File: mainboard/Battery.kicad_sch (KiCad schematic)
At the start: 23 parts, among them IC701 BQ21040DBV, IC702 MCP3425A2, Q701 BSS138, Q702 BSS84, X701 USB

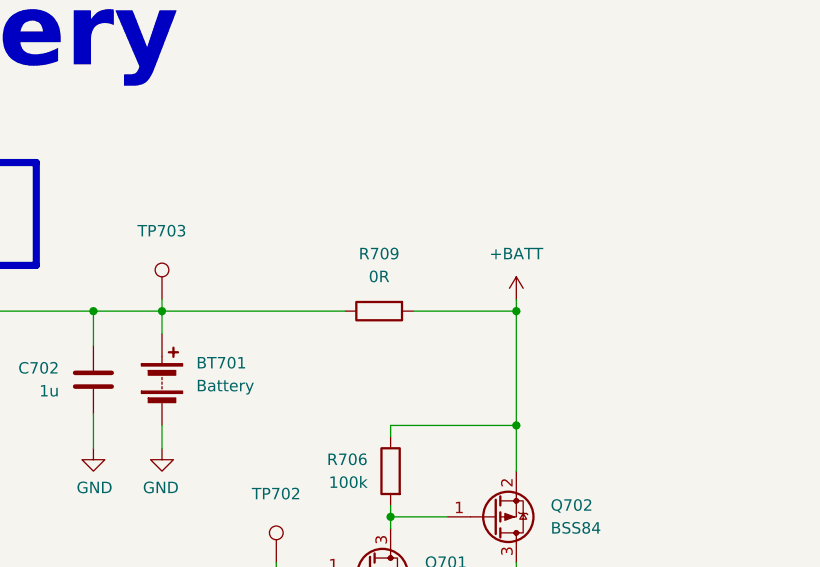
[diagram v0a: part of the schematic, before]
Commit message: Continue routing, add flash LEDs for the RGB camera, add PWM controller for the Display Backlight and the flash LEDs, add Polyfuse for the battery
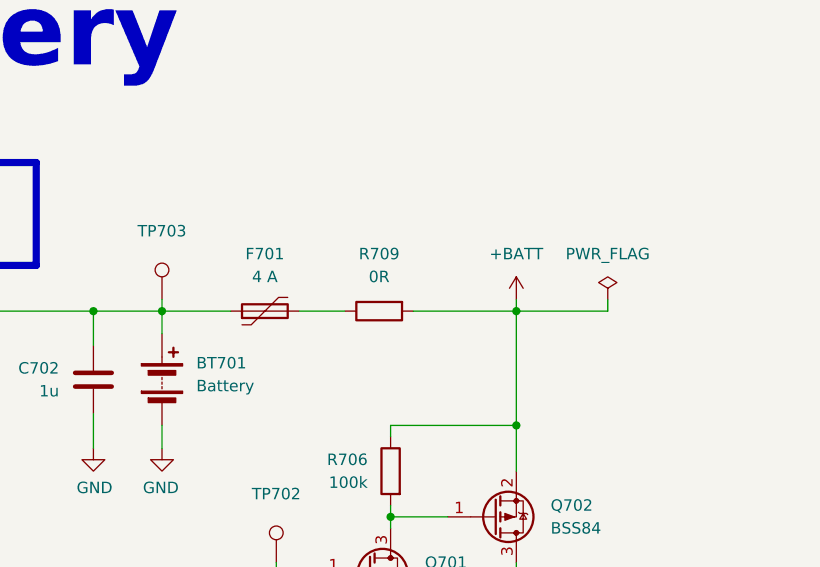
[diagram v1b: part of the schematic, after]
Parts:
- added F701: 4 A, Fuse:Fuse_1206_3216Metric, symbol Device:Polyfuse
- R709: footprint Resistor_SMD:R_0603_1608Metric -> Resistor_SMD:R_1206_3216Metric; manf (none) -> Bourns; manf# (none) -> CR1206-J/-000ELF; mouser# (none) -> 652-CR1206-J/-000ELF
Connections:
- net at BT701.1 (+), C702.1, IC701.2 (OUT)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: now also F701.1; no longer R709.1
- new net: F701.2, R709.1
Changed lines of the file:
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@@
 	(wire
 		(pts
-			(xy 193.04 50.8) (xy 213.36 50.8)
+			(xy 193.04 50.8) (xy 200.66 50.8)
 		)
 		(stroke
@@
 	(wire
 		(pts
+			(xy 208.28 50.8) (xy 213.36 50.8)
+		)
+		(stroke
+			(width 0)
+			(type default)
+		)
+	)
+	(wire
+		(pts
 			(xy 213.36 137.16) (xy 213.36 146.05)
 		)
@@
 	(wire
 		(pts
+			(xy 242.57 50.8) (xy 242.57 49.53)
+		)
+		(stroke
+			(width 0)
+			(type default)
+		)
+	)
+	(wire
+		(pts
 			(xy 97.79 82.55) (xy 97.79 81.28)
 		)
@@
 	(wire
 		(pts
+			(xy 232.41 50.8) (xy 242.57 50.8)
+		)
+		(stroke
+			(width 0)
+			(type default)
+		)
+	)
+	(wire
+		(pts
 			(xy 80.01 63.5) (xy 78.74 63.5)
 		)
@@
 	)
 	(symbol
+		(lib_id "power:PWR_FLAG")
+		(at 242.57 49.53 0)
+		(unit 1)
+		(exclude_from_sim no)
+		(in_bom yes)
+		(on_board yes)
+		(dnp no)
+		(fields_autoplaced yes)
+		(property "Reference" "#FLG0702"
+			(at 242.57 47.625 0)
+			(effects
+				(font
+					(size 1.27 1.27)
+				)
+				(hide yes)
+			)
+		)
+		(property "Value" "PWR_FLAG"
+			(at 242.57 44.45 0)
+			(effects
+				(font
+					(size 1.27 1.27)
+				)
+			)
+		)
+		(property "Footprint" ""
+			(at 242.57 49.53 0)
+			(effects
+				(font
+					(size 1.27 1.27)
+				)
+				(hide yes)
+			)
+		)
+		(property "Datasheet" "~"
+			(at 242.57 49.53 0)
+			(effects
+				(font
+					(size 1.27 1.27)
+				)
+				(hide yes)
+			)
+		)
+		(property "Description" "Special symbol for telling ERC where power comes from"
+			(at 242.57 49.53 0)
+			(effects
+				(font
+					(size 1.27 1.27)
+				)
+				(hide yes)
+			)
+		)
+		(pin "1"
+		)
+		(instances
+			(project "Mainboard"
+				(path "/d5742f03-3b1a-42e5-a384-018bd4b919aa/c5103ceb-5325-4a84-a025-9638a412984e/a86b9e25-5bc0-455f-833c-d00b4e9a8b22"
+					(reference "#FLG0702")
+					(unit 1)
+				)
+			)
+		)
+	)
+	(symbol
 		(lib_id "Device:R")
 		(at 132.08 60.96 0)
@@
 	)
 	(symbol
+		(lib_id "Device:Polyfuse")
+		(at 204.47 50.8 90)
+		(unit 1)
+		(exclude_from_sim no)
+		(in_bom yes)
+		(on_board yes)
+		(dnp no)
+		(fields_autoplaced yes)
+		(property "Reference" "F701"
+			(at 204.47 44.45 90)
+			(effects
+				(font
+					(size 1.27 1.27)
+				)
+			)
+		)
+		(property "Value" "4 A"
+			(at 204.47 46.99 90)
+			(effects
+				(font
+					(size 1.27 1.27)
+				)
+			)
+		)
+		(property "Footprint" "Fuse:Fuse_1206_3216Metric"
+			(at 209.55 49.53 0)
+			(effects
+				(font
+					(size 1.27 1.27)
+				)
+				(justify left)
+				(hide yes)
+			)
+		)
+		(property "Datasheet" "https://www.mouser.de/manufacturer/littelfuse/"
+			(at 204.47 50.8 0)
+			(effects
+				(font
+					(size 1.27 1.27)
+				)
+				(hide yes)
+			)
+		)
+		(property "Description" "Resettable fuse, polymeric positive temperature coefficient"
+			(at 204.47 50.8 0)
+			(effects
+				(font
+					(size 1.27 1.27)
+				)
+				(hide yes)
+			)
+		)
+		(property "manf" "Littelfuse"
+			(at 204.47 50.8 0)
+			(effects
+				(font
+					(size 1.27 1.27)
+				)
+				(hide yes)
+			)
+		)
+		(property "manf#" "1206L400SLWR"
+			(at 204.47 50.8 0)
+			(effects
+				(font
+					(size 1.27 1.27)
+				)
+				(hide yes)
+			)
+		)
+		(property "mouser#" "576-1206L400SLWR"
+			(at 204.47 50.8 0)
+			(effects
+				(font
+					(size 1.27 1.27)
+				)
+				(hide yes)
+			)
+		)
+		(property "CONFIG" ""
+			(at 204.47 50.8 0)
+			(effects
+				(font
+					(size 1.27 1.27)
+				)
+				(hide yes)
+			)
+		)
+		(pin "2"
+		)
+		(pin "1"
+		)
+		(instances
+			(project ""
+				(path "/d5742f03-3b1a-42e5-a384-018bd4b919aa/c5103ceb-5325-4a84-a025-9638a412984e/a86b9e25-5bc0-455f-833c-d00b4e9a8b22"
+					(reference "F701")
+					(unit 1)
+				)
+			)
+		)
+	)
+	(symbol
 		(lib_id "power:GND")
 		(at 213.36 146.05 0)
@@
 			)
 		)
-		(property "Footprint" "Resistor_SMD:R_0603_1608Metric"
+		(property "Footprint" "Resistor_SMD:R_1206_3216Metric"
 			(at 217.17 49.022 90)
 			(effects
@@
 			)
 		)
-		(property "Datasheet" "https://www.mouser.de/datasheet/2/54/cr-1858361.pdf"
+		(property "Datasheet" "https://www.mouser.de/datasheet/3/40/1/cr.pdf"
 			(at 217.17 50.8 0)
 			(effects
@@
 			)
 		)
-		(property "manf" ""
+		(property "manf" "Bourns"
 			(at 217.17 50.8 0)
 			(effects
@@
 			)
 		)
-		(property "manf#" ""
+		(property "manf#" "CR1206-J/-000ELF"
 			(at 217.17 50.8 0)
 			(effects
@@
 			)
 		)
-		(property "mouser#" ""
+		(property "mouser#" "652-CR1206-J/-000ELF"
 			(at 217.17 50.8 0)
 			(effects

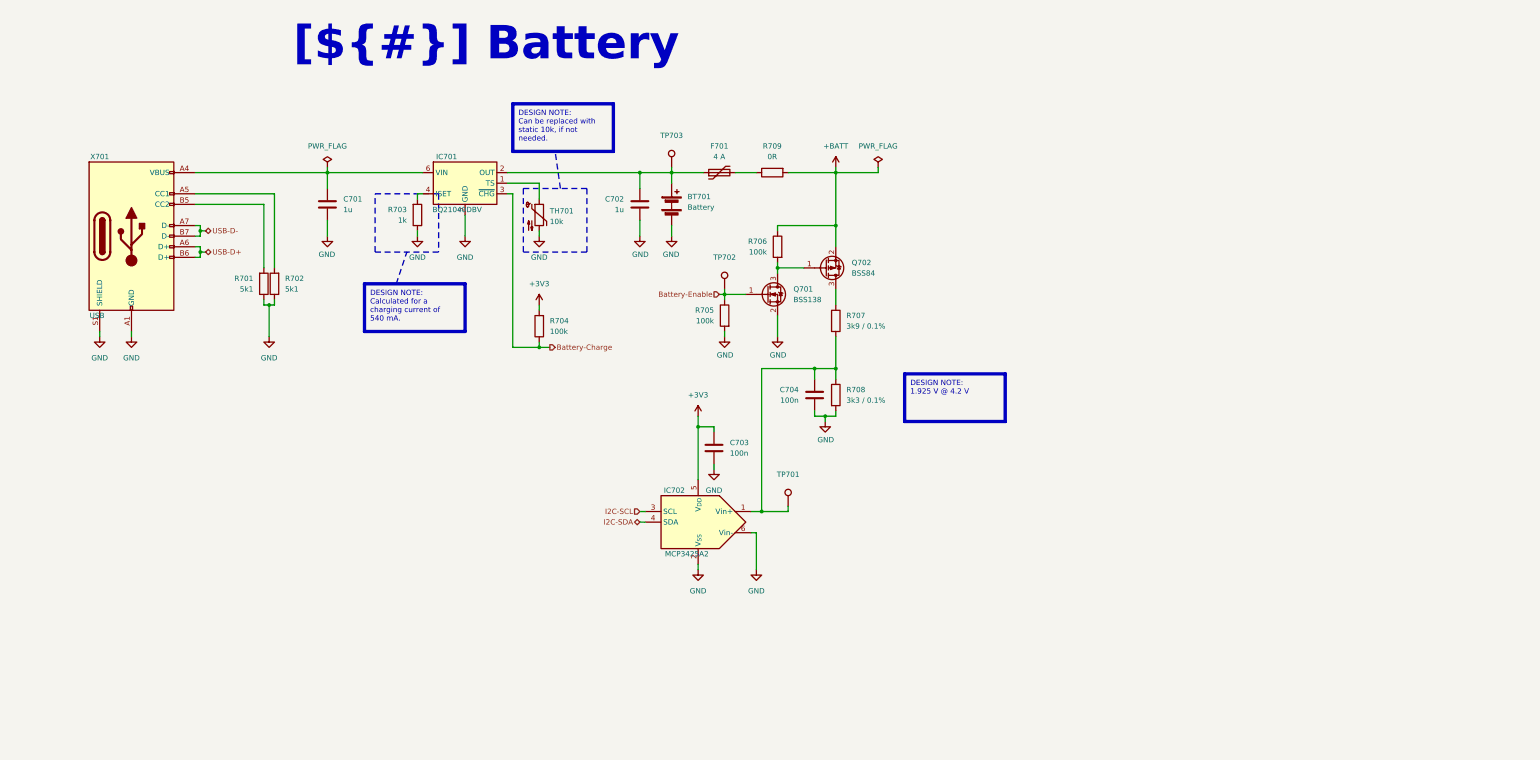
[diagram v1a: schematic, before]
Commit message: Remove ADC for battery measurement and add a fuel gauge
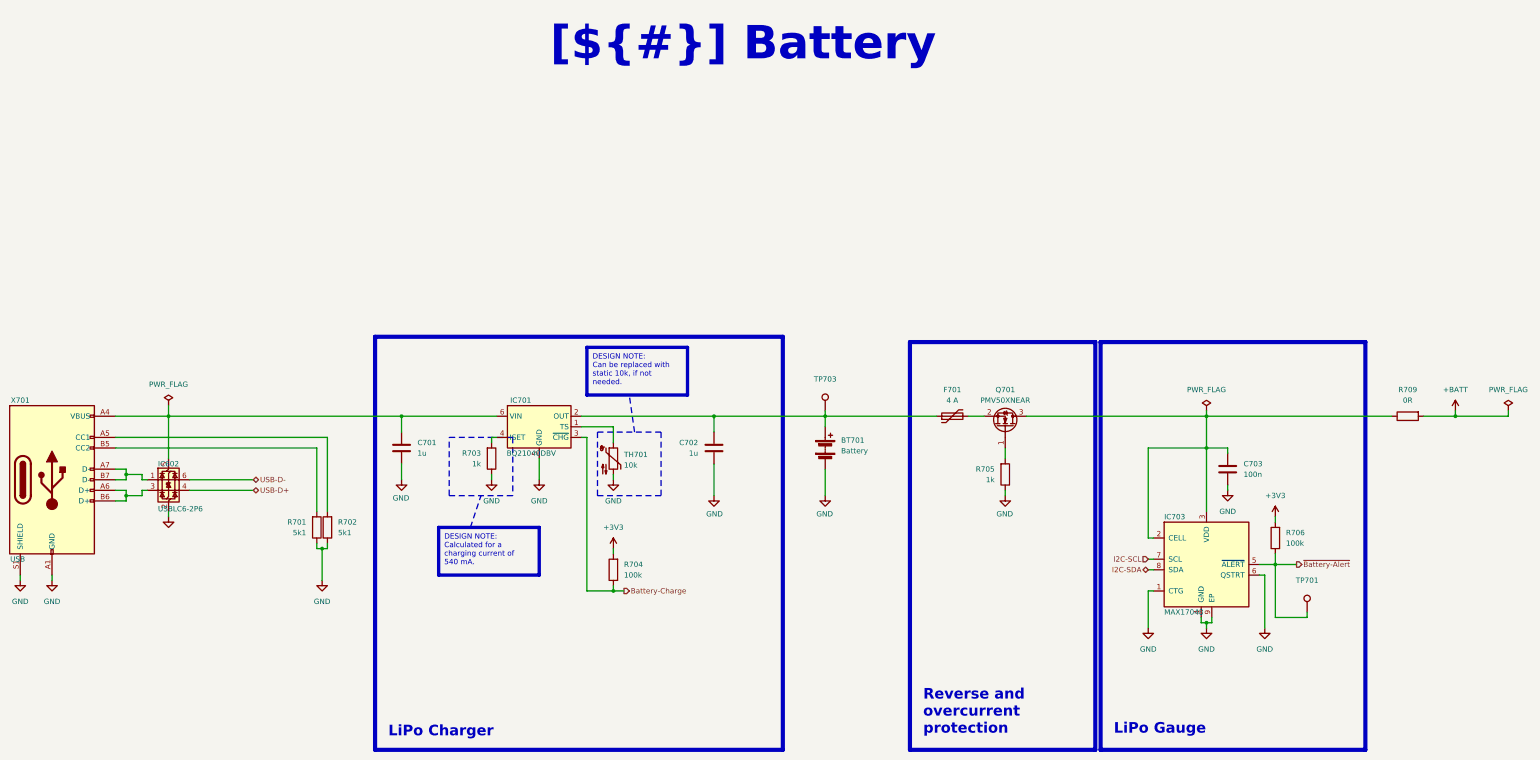
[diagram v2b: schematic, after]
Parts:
- removed C704: 100n, Capacitor_SMD:C_0603_1608Metric, symbol Device:C
- removed IC702: MCP3425A2, Package_TO_SOT_SMD:SOT-23-6, symbol Analog_ADC:MCP3425Axx-xCH
- removed Q701: BSS138, Package_TO_SOT_SMD:SOT-23, symbol Transistor_FET:BSS138
- removed Q702: BSS84, Package_TO_SOT_SMD:SOT-23, symbol Transistor_FET:BSS84
- removed R707: 3k9 / 0.1%, Resistor_SMD:R_0603_1608Metric, symbol Device:R
- removed R708: 3k3 / 0.1%, Resistor_SMD:R_0603_1608Metric, symbol Device:R
- removed TP702: ~, TestPoint:TestPoint_Pad_1.0x1.0mm, symbol Connector:TestPoint
- added IC602: USBLC6-2P6, Package_TO_SOT_SMD:SOT-666, symbol Power_Protection:USBLC6-2P6
- added IC703: MAX17048, Package_DFN_QFN:TDFN-8-1EP_2x2mm_P0.5mm_EP0.8x1.2mm, symbol Maxim:MAX17048
- added Q701: PMV50XNEAR, Package_TO_SOT_SMD:SOT-23, symbol Nexperia:PMV50XNEAR
- R705: value 100k -> 1k; manf# CR0603-JW-104ELF -> CR0603-JW-102ELF; mouser# 652-CR0603-JW-104ELF -> 652-CR0603-JW-102ELF
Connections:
- net Battery-Enable is gone; now on net GND: R705.1
- net +3V3: now also R706.2; no longer C703.1
- net +BATT: no longer R706.1
- net GND: now also IC602.2 (GND), IC703.1 (CTG), IC703.4 (GND), IC703.6 (QSTRT), IC703.9 (EP); no longer R705.2
- net I2C-SCL: now also IC703.7 (SCL)
- net I2C-SDA: now also IC703.8 (SDA)
- net USB-D+: now also IC602.4 (I/O2); no longer X701.A6 (D+), X701.B6 (D+)
- net USB-D-: now also IC602.6 (I/O1); no longer X701.A7 (D-), X701.B7 (D-)
- net ~{Battery-Alert}: now reaches TP701.1
- net ~{Battery-Alert}: now also R706.1, IC703.5 (~{ALERT})
- net at C701.1, IC701.6 (VIN), X701.A4 (VBUS)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: now also IC602.5 (VBUS)
- net at F701.2: now also Q701.2 (S); no longer R709.1
- new net: IC602.1 (I/O1), X701.A7 (D-), X701.B7 (D-)
- new net: IC602.3 (I/O2), X701.A6 (D+), X701.B6 (D+)
- new net: Q701.1 (G), R705.2
- new net: C703.1, IC703.2 (CELL), IC703.3 (VDD), Q701.3 (D), R709.1
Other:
- moved on the sheet: BT701, C701, C702, F701, IC701, R701, R702, R703, R704, R709, TH701, TP703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

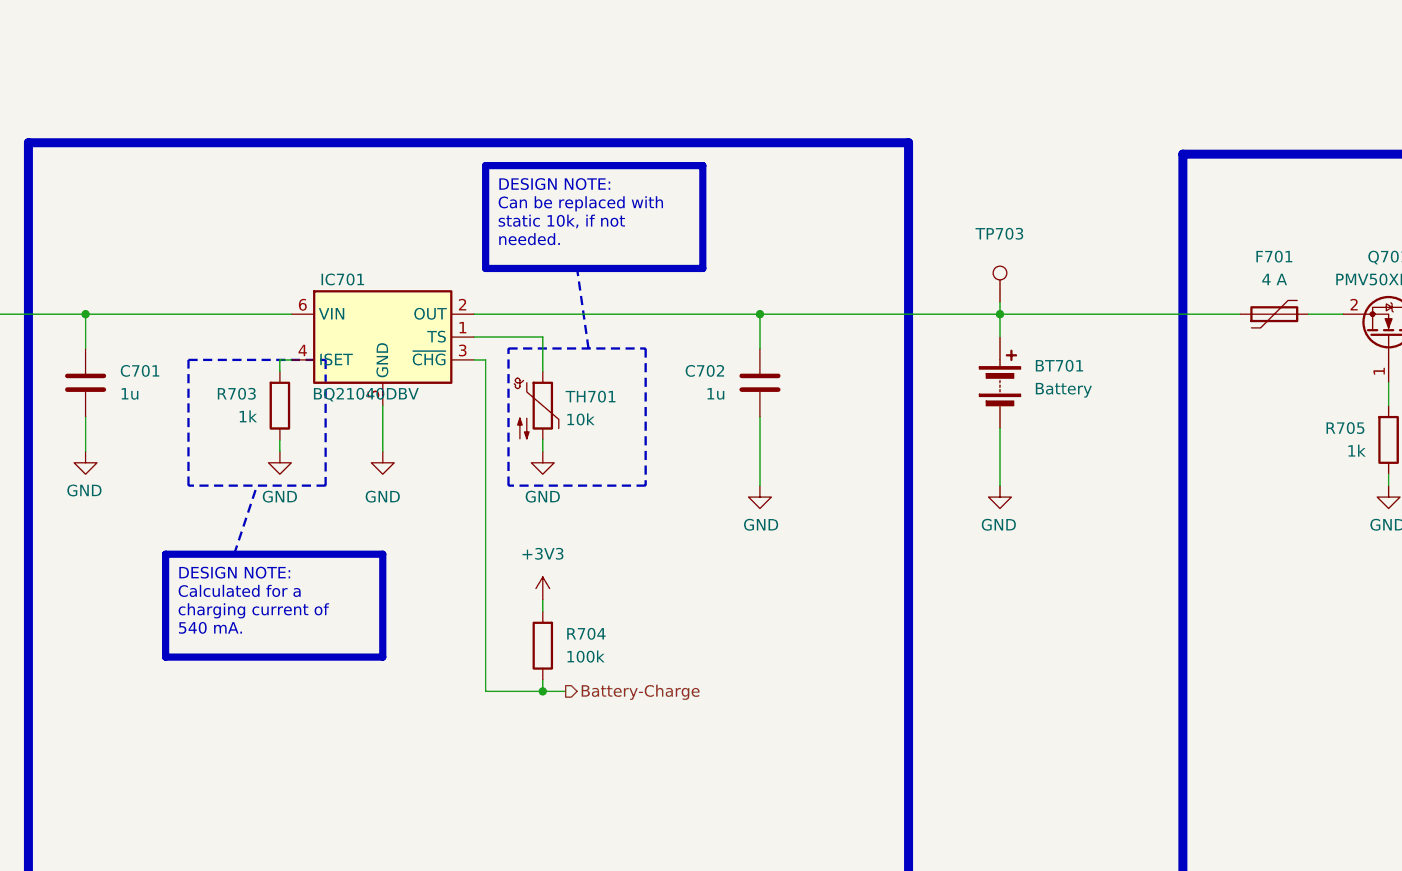
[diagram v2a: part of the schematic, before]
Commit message: Replace temperature sensor and optimize the position, replace LiPo battery with a flat one
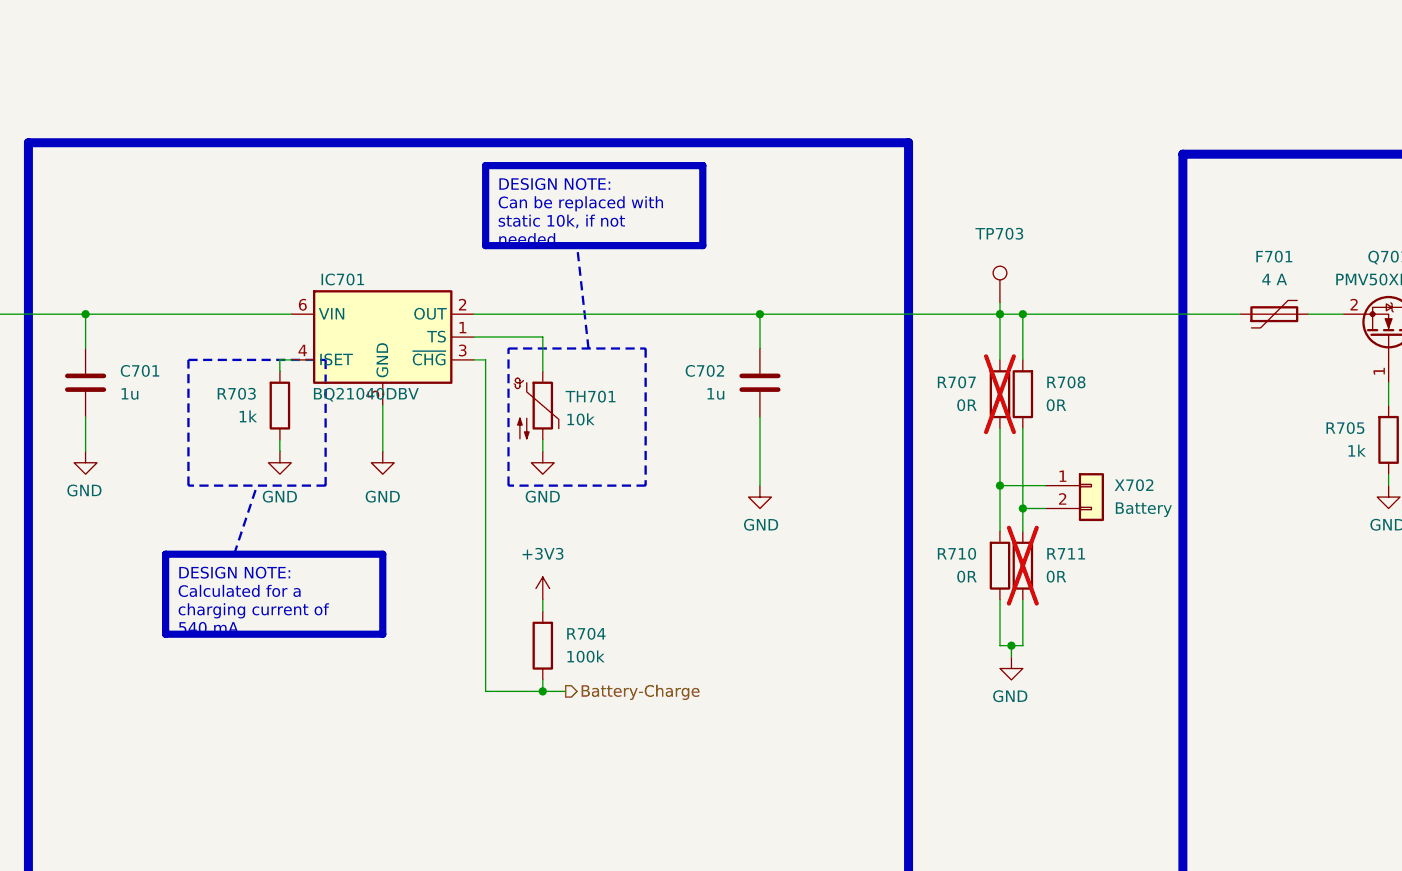
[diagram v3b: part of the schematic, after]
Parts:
- removed BT701: Battery, Battery_Kampi:Keystone_18650, symbol Device:Battery
- added R707, R708, R710, R711: 0R, Resistor_SMD:R_1206_3216Metric, symbol Device:R
- added X702: Battery, Connector_JST:JST_PH_B2B-PH-SM4-TB_1x02-1MP_P2.00mm_Vertical, symbol Connector_Generic:Conn_01x02
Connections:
- net GND: now also R710.1, R711.2
- net at C702.1, F701.1, IC701.2 (OUT)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: now also R707.2, R708.2
- new net: R707.1, R710.2, X702.1 (Pin_1)
- new net: R708.1, R711.1, X702.2 (Pin_2)

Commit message: Layout complete
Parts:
- F701: value 4 A -> 6 V / 4.5 A; manf# 1206L400SLWR -> 1206L450SLWR; mouser# 576-1206L400SLWR -> 576-1206L450SLWR
- Q701: value PMV50XNEAR -> Si2333CDS; footprint Package_TO_SOT_SMD:SOT-23 -> Package_TO_SOT_SMD:SOT-23-3; symbol Nexperia:PMV50XNEAR -> Vishay:Si2333CDS; manf Nexperia -> Vishay / Siliconix; manf# PMV50XNEAR -> SI2333CDS-T1-BE3; mouser# 771-PMV50XNEAR -> 78-SI2333CDS-T1-BE3
- X702: footprint Connector_JST:JST_PH_B2B-PH-SM4-TB_1x02-1MP_P2.00mm_Vertical -> JST:S2B-PH-SM4-TB; manf# B2B-PH-SM4-TB(LF)(SN) -> S2B-PH-SM4-TB(LF)(SN); mouser# 306-B2BPHSM4TBLFSN -> 306-S2B-PH-SM4-TB(LF)(SN)
- renumbered IC602 to IC701, IC701 to IC702, R707 to R705, R710 to R706, R708 to R707, R711 to R708, R705 to R709, R706 to R710, R709 to R711, TP703 to TP701, TP701 to TP702
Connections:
- net at Q701.2 (S): now also C703.1, IC703.2 (CELL), IC703.3 (VDD), R711.1; no longer F701.2
- new net: F701.2, Q701.3 (D)
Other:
- moved on the sheet: C703, F701, IC703, Q701, R709, R710, TP702

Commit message: Release 1.0.0
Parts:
- TP701: footprint TestPoint:TestPoint_Pad_1.0x1.0mm -> Testpoints_Kampi:TestPoint_Pad_1.0x1.0mm
- TP702: footprint TestPoint:TestPoint_Pad_1.0x1.0mm -> Testpoints_Kampi:TestPoint_Pad_1.0x1.0mm; now not fitted
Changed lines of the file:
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@@
 			)
 		)
-		(property "Footprint" "TestPoint:TestPoint_Pad_1.0x1.0mm"
+		(property "Footprint" "Testpoints_Kampi:TestPoint_Pad_1.0x1.0mm"
 			(at 234.95 107.95 0)
 			(effects
@@
 		(in_bom no)
 		(on_board yes)
-		(dnp no)
+		(dnp yes)
 		(property "Reference" "TP702"
 			(at 349.25 148.59 0)
@@
 			)
 		)
-		(property "Footprint" "TestPoint:TestPoint_Pad_1.0x1.0mm"
+		(property "Footprint" "Testpoints_Kampi:TestPoint_Pad_1.0x1.0mm"
 			(at 354.33 156.21 0)
 			(effects

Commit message: Task: Issue #7
- Increase the width of the cutout for the temperature sensor
- Add missing component informations
- Fix wrong component informations

Closes: #7

Signed-off-by: Daniel Kampert <DanielKampert@kampis-elektroecke.de>
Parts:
- R706, R707, R711: manf# CR1206-J/-000ELF -> CR0603-J/-000ELF
- TH701: manf TDK -> YAGEO; manf# NTCG163JF103FT1H -> RC0603FR-073K3L; mouser# 810-NTCG163JF103FT1H -> 603-RC0603FR-073K3L
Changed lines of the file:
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@@
 			)
 		)
-		(property "manf#" "CR1206-J/-000ELF"
+		(property "manf#" "CR0603-J/-000ELF"
 			(at 229.87 137.16 0)
 			(effects
@@
 			)
 		)
-		(property "manf#" "CR1206-J/-000ELF"
+		(property "manf#" "CR0603-J/-000ELF"
 			(at 232.41 118.11 0)
 			(effects
@@
 			)
 		)
-		(property "Description" "Temperature dependent resistor, negative temperature coefficient"
+		(property "Description" "Resistor"
 			(at 179.07 119.38 0)
 			(effects
@@
 			)
 		)
-		(property "manf" "TDK"
+		(property "manf" "YAGEO"
 			(at 179.07 119.38 0)
 			(effects
@@
 			)
 		)
-		(property "manf#" "NTCG163JF103FT1H"
+		(property "manf#" "RC0603FR-073K3L"
 			(at 179.07 119.38 0)
 			(effects
@@
 			)
 		)
-		(property "mouser#" "810-NTCG163JF103FT1H"
+		(property "mouser#" "603-RC0603FR-073K3L"
 			(at 179.07 119.38 0)
 			(effects
@@
 			)
 		)
-		(property "manf#" "CR1206-J/-000ELF"
+		(property "manf#" "CR0603-J/-000ELF"
 			(at 369.57 109.22 0)
 			(effects

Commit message: Add feedback from PCBWay
Signed-off-by: Daniel Kampert <DanielKampert@kampis-elektroecke.de>
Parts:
- IC703: manf# 700-MAX17048G+T10 -> MAX17048G+T10
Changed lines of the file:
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@@
 			)
 		)
-		(property "manf#" "700-MAX17048G+T10"
+		(property "manf#" "MAX17048G+T10"
 			(at 325.12 144.78 0)
 			(effects
